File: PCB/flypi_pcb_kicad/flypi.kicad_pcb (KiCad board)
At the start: 2 copper layers, 76.1 x 85 mm, 45 parts, among them CON1 BARREL_JACK, J12 USB_A, P1 PeltS1S2, P10 RGB GB-R, P3 Fan-+, P4 Therm -s+, P5 HP1+-, P6 HP2-+, P7 servo -s+, P8 Ring s-+, P9 I2C +-scsd, Q1 1A_NPN_EBC, Q2 1A-NPN-EBC, Q3 1A_NPN_EBC, Q4 1A_NPN_EBC, U1 LM2596, U2 LM2596, U4 L298N, U5 arduino_mini

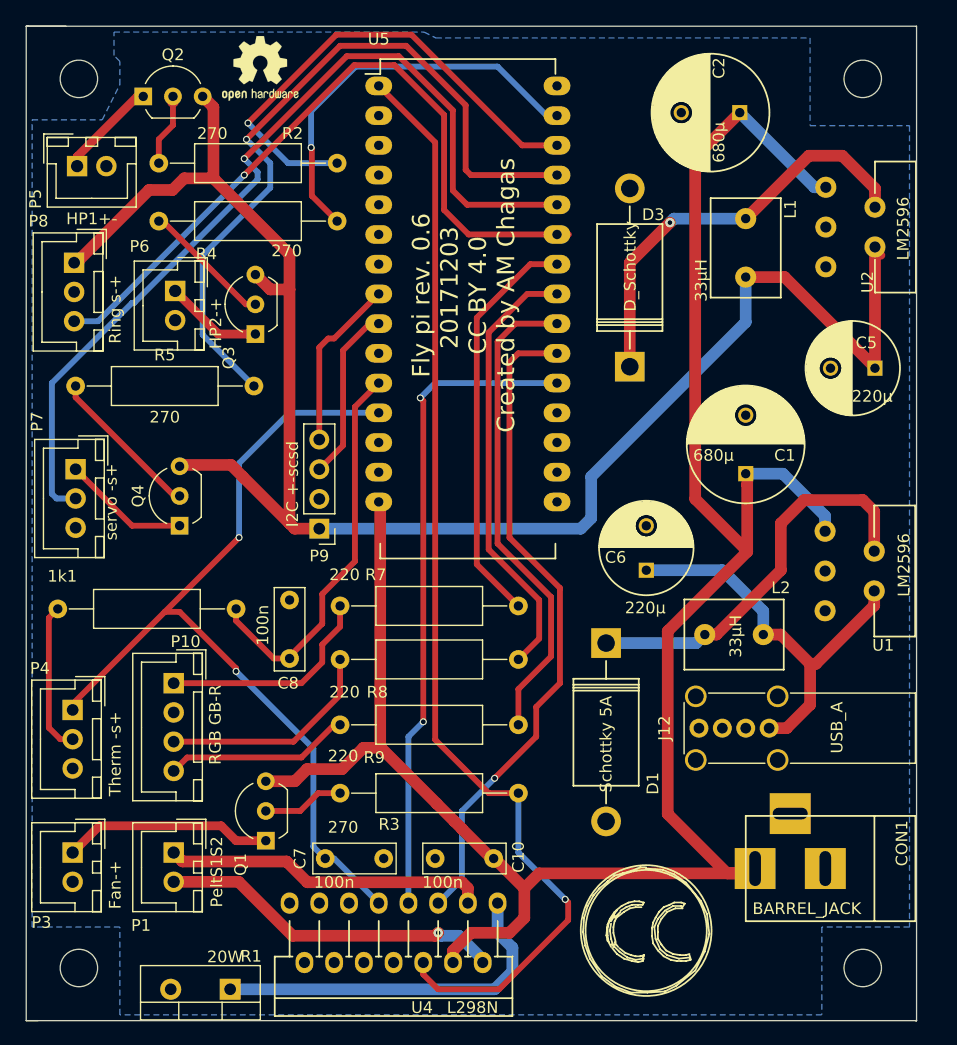
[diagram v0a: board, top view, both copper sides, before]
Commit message: update PCB, change resistor values: 220 for 270, change resistor footprints (shorter footprint), re-wire npn transistors -> now (-) side is being switched on/off, add some logos, change board license (from CC BY SA to CERN OHL 1.2), update board version 0.7 to 1.0 (as they are not backward compatible anymore)
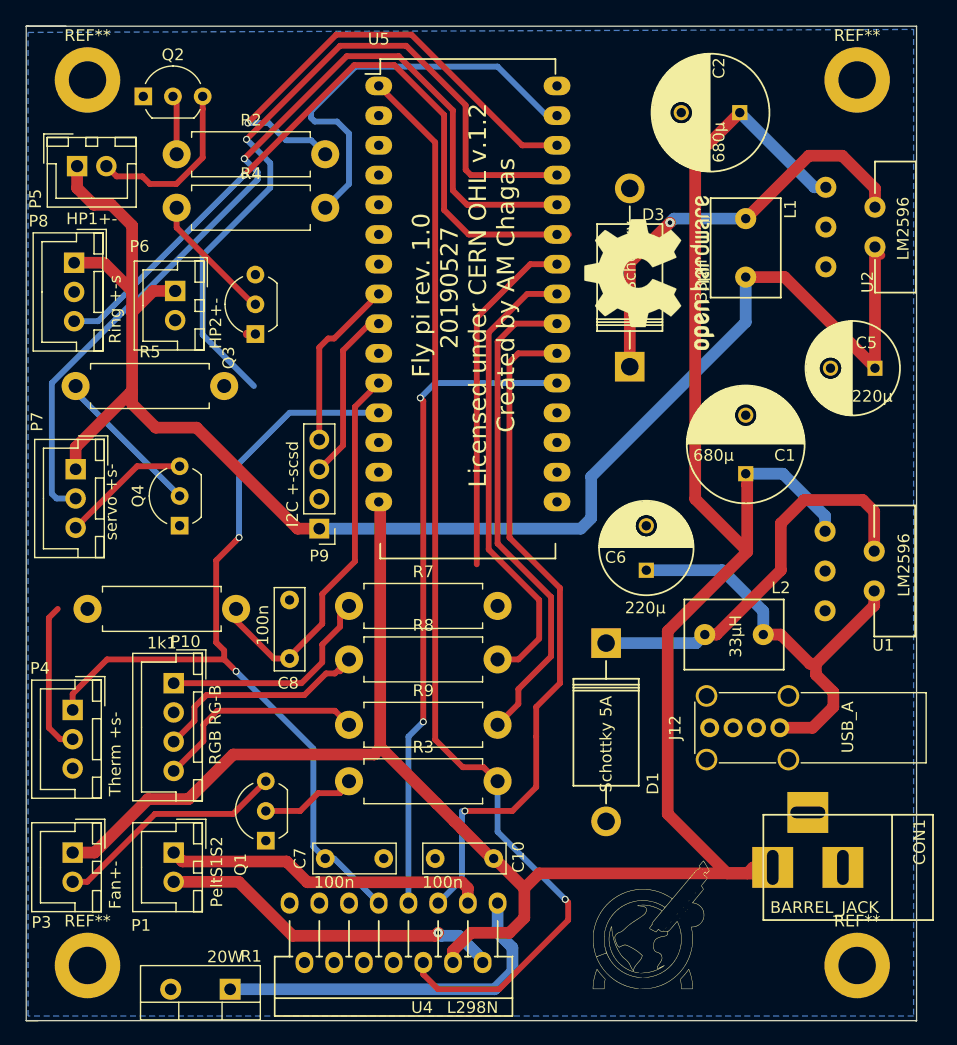
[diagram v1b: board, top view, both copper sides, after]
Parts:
- removed  : , Mounting_Holes:MountingHole_3.2mm_M3_DIN965
- removed ? (x3): , Mounting_Holes:MountingHole_3.2mm_M3_DIN965
- removed ?: , Symbols:OSHW-Logo2_7.3x6mm_SilkScreen
- removed ?: , Symbols:Symbol_CreativeCommons_SilkScreenTop_Type2_Big
- added G***: LOGO, footprints:LOGO, F.Cu at (158.2, 126.0)
- added REF**: MountingHole_3.2mm_M3_DIN965_Pad, MountingHole:MountingHole_3.2mm_M3_DIN965_Pad, F.Cu at (176.0, 129.3)
- added REF**: MountingHole_3.2mm_M3_DIN965_Pad, MountingHole:MountingHole_3.2mm_M3_DIN965_Pad, F.Cu at (176.0, 53.6)
- added REF**: MountingHole_3.2mm_M3_DIN965_Pad, MountingHole:MountingHole_3.2mm_M3_DIN965_Pad, F.Cu at (110.2, 53.6)
- added REF**: MountingHole_3.2mm_M3_DIN965_Pad, MountingHole:MountingHole_3.2mm_M3_DIN965_Pad, F.Cu at (110.2, 129.3)
- added REF**: OSHW-Logo2_14.6x12mm_SilkScreen, Symbol:OSHW-Logo2_14.6x12mm_SilkScreen, F.Cu at (158.2, 70.1)
- 1k1, R2, R3, R4, R5: footprint Resistors_THT:R_Axial_DIN0309_L9.0mm_D3.2mm_P15.24mm_Horizontal -> Resistor_THT:R_Axial_DIN0411_L9.9mm_D3.6mm_P12.70mm_Horizontal
- P10: value RGB GB-R -> RGB RG-B
- P3: value Fan-+ -> Fan+-
- P4: value Therm -s+ -> Therm +s-
- P6: value HP2-+ -> HP2+-
- P7: value servo -s+ -> servo +s-
- P8: value Ring s-+ -> Ring +-s
- R7, R8, R9: value 220 -> 270; footprint Resistors_THT:R_Axial_DIN0309_L9.0mm_D3.2mm_P15.24mm_Horizontal -> Resistor_THT:R_Axial_DIN0411_L9.9mm_D3.6mm_P12.70mm_Horizontal
- moved R4 1.91 mm to (117.9, 64.5)
- moved R2 1.70 mm to (117.9, 59.9)
- moved CON1 1.51 mm to (175.0, 120.9)
- moved R3 1.27 mm to (132.6, 113.5)
- moved J12 0.92 mm to (169.4, 109.0)
- moved R7 0.76 mm to (132.6, 98.6)
- moved R8 0.76 mm to (132.6, 103.1)
- moved R9 0.76 mm to (132.6, 108.7)
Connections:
- J12 pad 2: Net-(J12-Pad2) -> (no net)
- J12 pad 3: Net-(J12-Pad3) -> (no net)
- P3 pad 1: Net-(P3-Pad1) -> Net-(C1-Pad1)
- P3 pad 2: GND -> Net-(P3-Pad2)
- P5 pad 1: Net-(P5-Pad1) -> Net-(C5-Pad1)
- P5 pad 2: GND -> Net-(P5-Pad2)
- P6 pad 1: Net-(P6-Pad1) -> Net-(C5-Pad1)
- P6 pad 2: GND -> Net-(P6-Pad2)
- P7 pad 1: Net-(P7-Pad1) -> Net-(C5-Pad1)
- P7 pad 3: GND -> Net-(P7-Pad3)
- Q1 pad 1: Net-(P3-Pad1) -> GND
- Q1 pad 3: Net-(C1-Pad1) -> Net-(P3-Pad2)
- Q2 pad 1: Net-(P5-Pad1) -> GND
- Q2 pad 3: Net-(C5-Pad1) -> Net-(P5-Pad2)
- Q3 pad 1: Net-(P6-Pad1) -> GND
- Q3 pad 3: Net-(C5-Pad1) -> Net-(P6-Pad2)
- Q4 pad 1: Net-(P7-Pad1) -> GND
- Q4 pad 3: Net-(C5-Pad1) -> Net-(P7-Pad3)
- U4 pad 10: Net-(U4-Pad10) -> (no net)
- U4 pad 11: Net-(U4-Pad11) -> (no net)
- U4 pad 12: Net-(U4-Pad12) -> (no net)
- U4 pad 13: Net-(U4-Pad13) -> (no net)
- U4 pad 14: Net-(U4-Pad14) -> (no net)
- U4 pad 15: Net-(U4-Pad15) -> (no net)
- U5 pad 10: Net-(U5-Pad10) -> (no net)
- U5 pad 13: Net-(U5-Pad13) -> (no net)
- U5 pad 16: Net-(U5-Pad16) -> (no net)
- U5 pad 17: Net-(U5-Pad17) -> (no net)
- U5 pad 18: Net-(U5-Pad18) -> (no net)
- U5 pad 2: Net-(U5-Pad2) -> (no net)
- U5 pad 3: Net-(U5-Pad3) -> (no net)
- U5 pad 30: Net-(U5-Pad30) -> (no net)
- U5 pad 4: Net-(U5-Pad4) -> (no net)
- U5 pad 5: Net-(U5-Pad5) -> (no net)
- U5 pad 6: Net-(U5-Pad6) -> (no net)
- U5 pad 7: Net-(U5-Pad7) -> (no net)
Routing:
- net Net-(C1-Pad1): track 182.8 -> 204.2 mm
- net Net-(P3-Pad2): track 0.00 -> 20.1 mm
- net Net-(P3-Pad1): track 18.0 -> 0.00 mm
- net Net-(P5-Pad2): track 0.00 -> 15.0 mm
- net Net-(P7-Pad3): track 0.00 -> 11.4 mm
- net Net-(P7-Pad1): track 10.9 -> 0.00 mm
- net Net-(C5-Pad1): track 147.7 -> 137.8 mm
- net Net-(P6-Pad1): track 9.08 -> 0.00 mm
- net Net-(P5-Pad1): track 8.59 -> 0.00 mm
- net Net-(R7-Pad2): track 34.9 -> 29.8 mm
- net Net-(U4-Pad5): track 56.7 -> 59.4 mm
- net Net-(P10-Pad4): track 15.9 -> 18.4 mm
- net Net-(Q2-Pad2): track 7.13 -> 5.07 mm
- net Net-(P10-Pad3): track 18.9 -> 20.9 mm
- net Net-(C6-Pad1): track 35.1 -> 36.9 mm
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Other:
- board text added: "Fly pi rev. 1.0 20190527 Licensed under CERN OHL v.1.2 Created by AM Chagas"
- board text removed: "Fly pi rev. 0.6 20171203 CC BY 4.0 Created by AM Chagas"
